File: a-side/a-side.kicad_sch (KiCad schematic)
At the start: 39 parts, among them IC1 GL823K, IC2 GL823K, J1 Conn_01x04, J2 503500-0993, J3 503500-0993, J4 USB_A, J5 USB_A, U1 AMS1117CD-3.3, U2 SRV05-4, Y1 Crystal

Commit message: sorrryyy
this is a commit from last night, started layout, fixed schematic issues and well. ready to fix problems now
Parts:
- removed J2, J3: 503500-0993, 5035000993:5035000993, symbol 503500-0993:503500-0993
- added J6, J7: SD_Card_Receptacle, symbol Connector:SD_Card_Receptacle
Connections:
- net GND: now also J6.3 (VSS), J6.6 (VSS), J7.3 (VSS), J7.6 (VSS)
- net SD1_CLK: now also J6.5 (CLK)
- net SD1_CMD: now also J6.2 (CMD)
- net SD1_D0: now also J6.7 (DAT0)
- net SD1_D1: now also J6.8 (DAT1)
- net SD1_D2: now also J6.9 (DAT2)
- net SD1_D3: now also J6.1 (CD/DAT3)
- net SD1_PWR: now also J6.4 (VDD), J7.4 (VDD)
- net USB_DM: now also U2.6 (IO4)
- net USB_DP: now also U2.4 (IO3)
- no-connect marks 23 -> 13

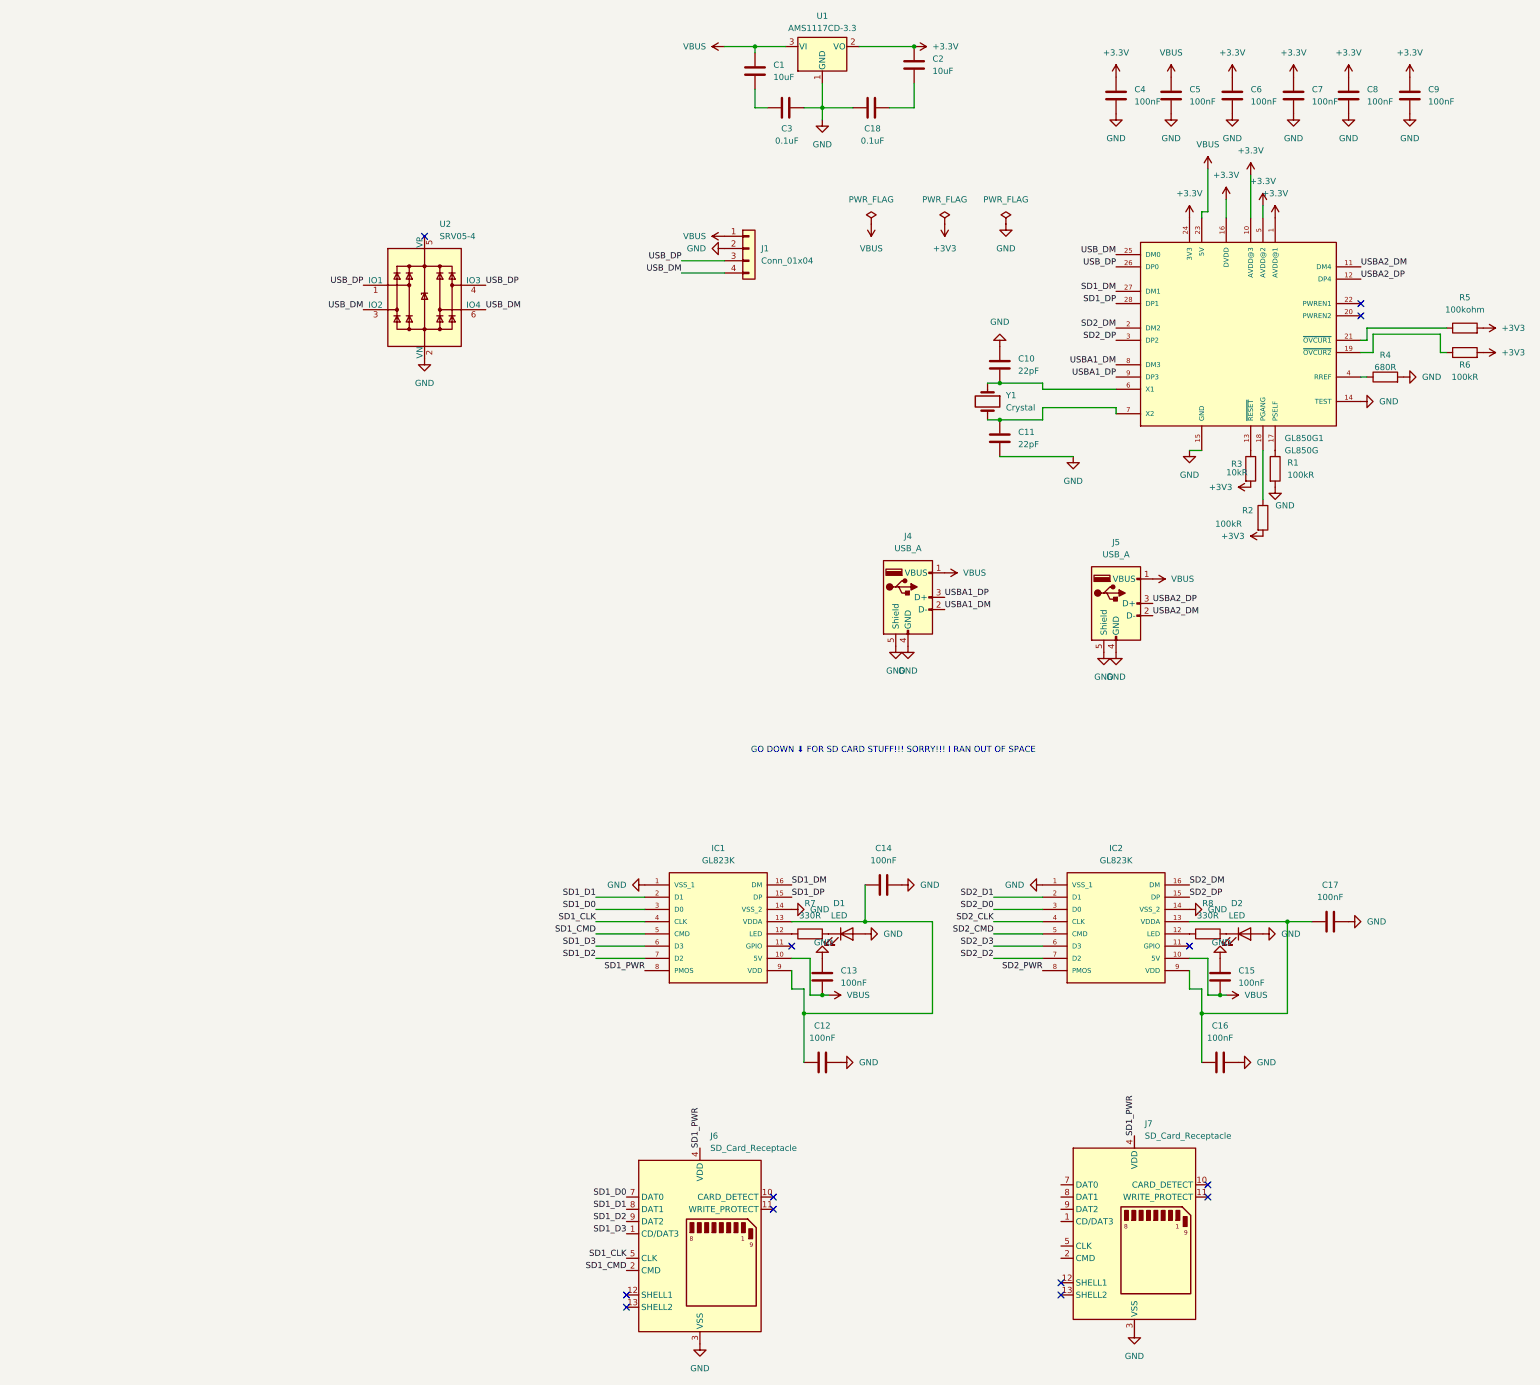
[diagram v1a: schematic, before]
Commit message: comitttt
fixed most of the problems stated yesterday, NC's on your ESD protection is a red flag, VCC and differentials should bridge the 2 ESD pins
C3 and C18 aren't done properly and should be in parallel to the AMS1117
All my footprints are buns and not from KiCad library
SD data pins are wired to the mounting pins...
And I should probably consider not using a connector for the upstream but rather a usbc-usbc wire to connect the two.

YEAH WHATEVER JUST IGNORE THAT theyre mostly fineeee ig ill go home and finish.
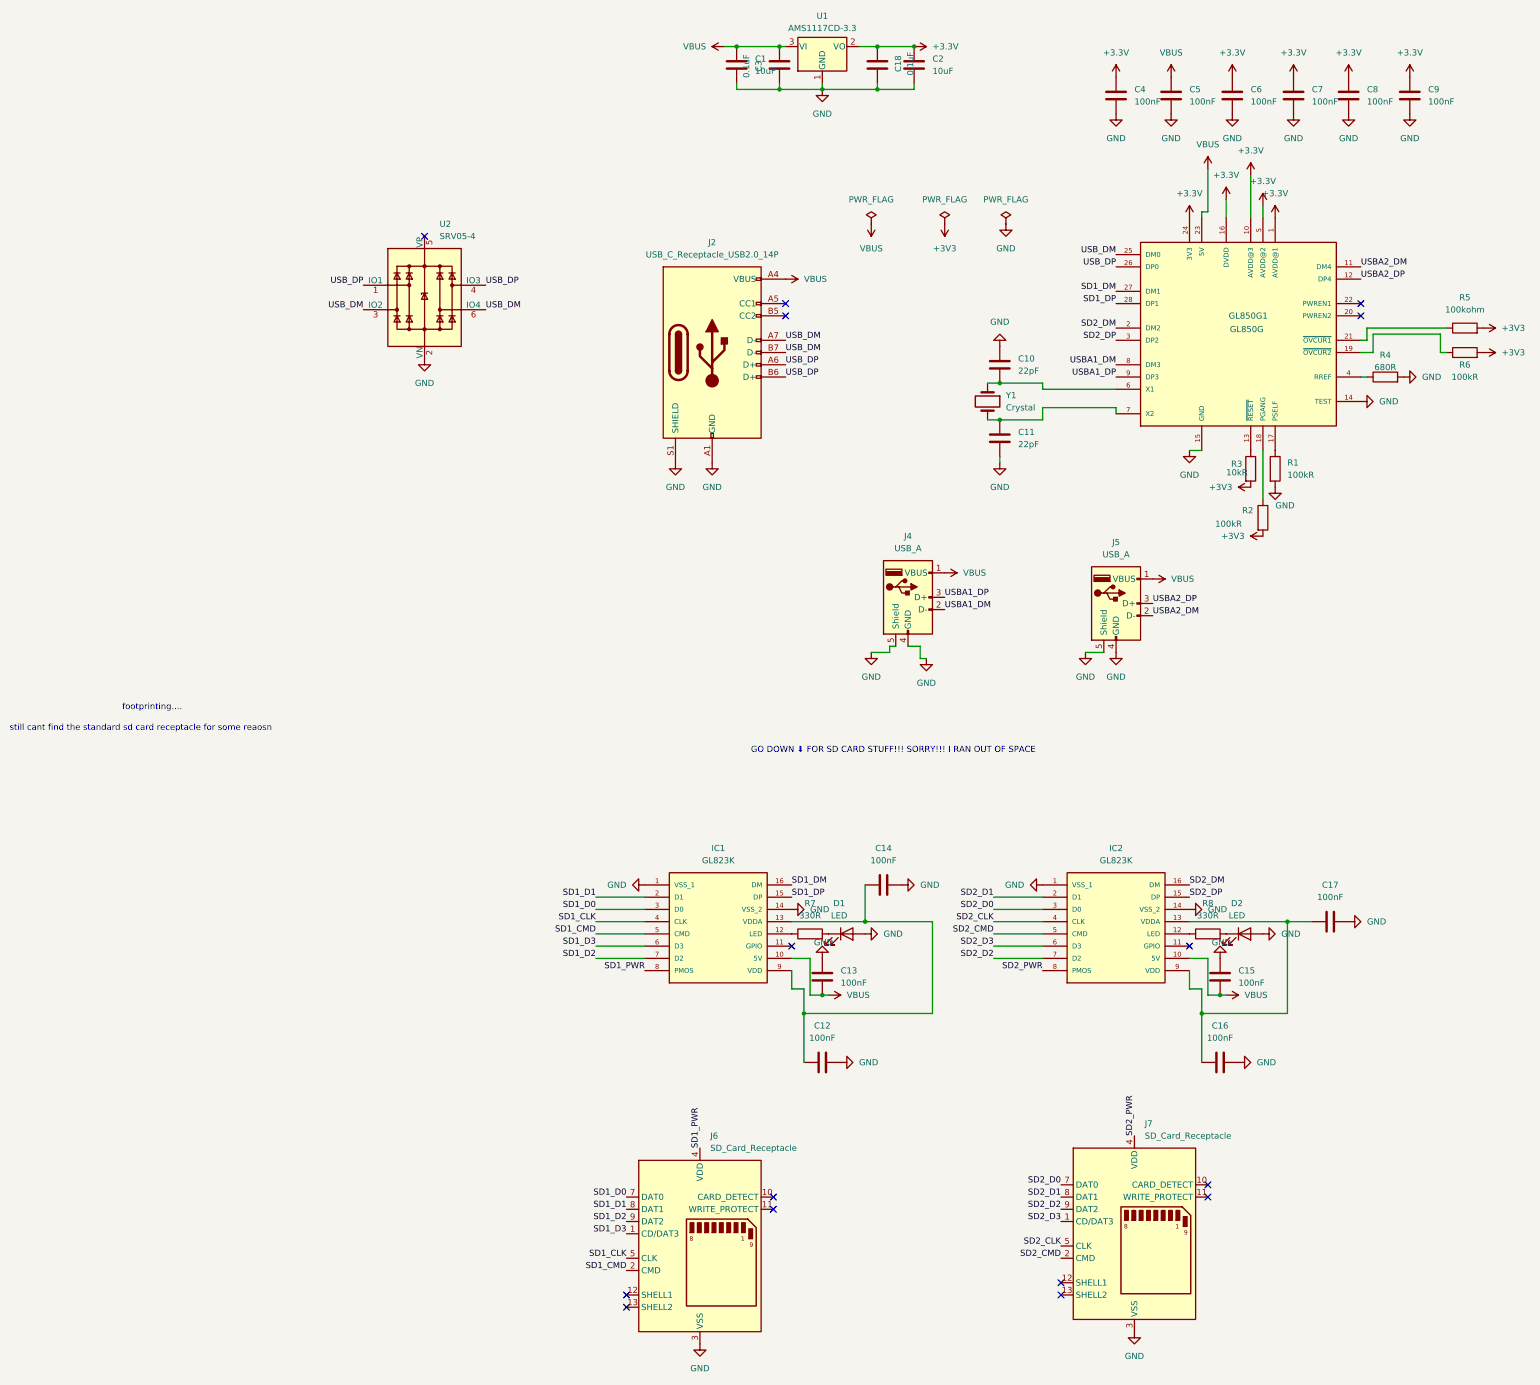
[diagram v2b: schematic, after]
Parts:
- removed J1: Conn_01x04, Connector_PinHeader_2.54mm:PinHeader_1x04_P2.54mm_Vertical, symbol Connector_Generic:Conn_01x04
- added J2: USB_C_Receptacle_USB2.0_14P, Connector_USB:USB_C_Receptacle_GCT_USB4105-xx-A_16P_TopMnt_Horizontal, symbol Connector:USB_C_Receptacle_USB2.0_14P
- J6, J7: footprint (none) -> Connector_Card:SD_TE_2041021
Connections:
- net +3.3V: now also C18.2
- net GND: now also C1.2, C2.2, J2.A1 (GND), J2.A12 (GND), J2.B1 (GND), J2.B12 (GND), J2.S1 (SHIELD)
- net SD1_PWR: no longer J7.4 (VDD)
- net SD2_CLK: now also J7.5 (CLK)
- net SD2_CMD: now also J7.2 (CMD)
- net SD2_D0: now also J7.7 (DAT0)
- net SD2_D1: now also J7.8 (DAT1)
- net SD2_D2: now also J7.9 (DAT2)
- net SD2_D3: now also J7.1 (CD/DAT3)
- net SD2_PWR: now also J7.4 (VDD)
- net USB_DM: now also J2.A7 (D-), J2.B7 (D-)
- net USB_DP: now also J2.A6 (D+), J2.B6 (D+)
- net VBUS: now also C3.1, J2.A4 (VBUS), J2.A9 (VBUS), J2.B4 (VBUS), J2.B9 (VBUS)
- no-connect marks 13 -> 15
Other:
- note added: "footprinting...."
- note added: "still cant find the standard sd card receptacle for some reaosn"
- moved on the sheet: C1, C3
